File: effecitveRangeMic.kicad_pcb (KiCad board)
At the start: 2 copper layers, 24.4 x 18 mm, 25 parts, among them J1 MicHeader

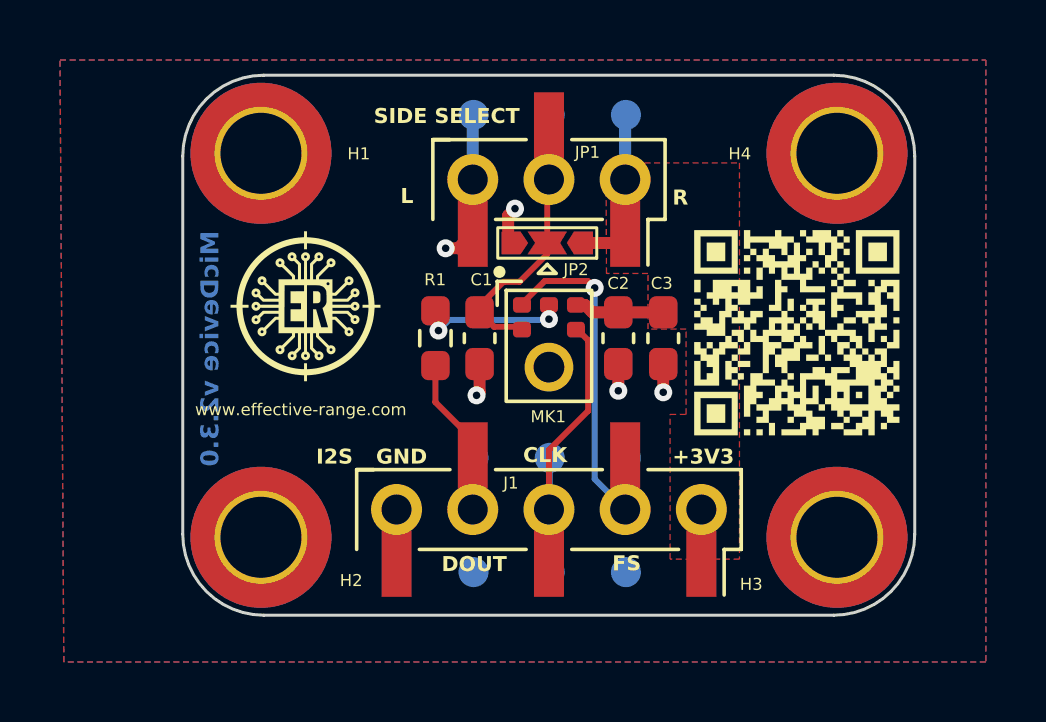
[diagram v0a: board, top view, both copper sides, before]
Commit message: Bumping release from 2.3.0 to 2.3.1
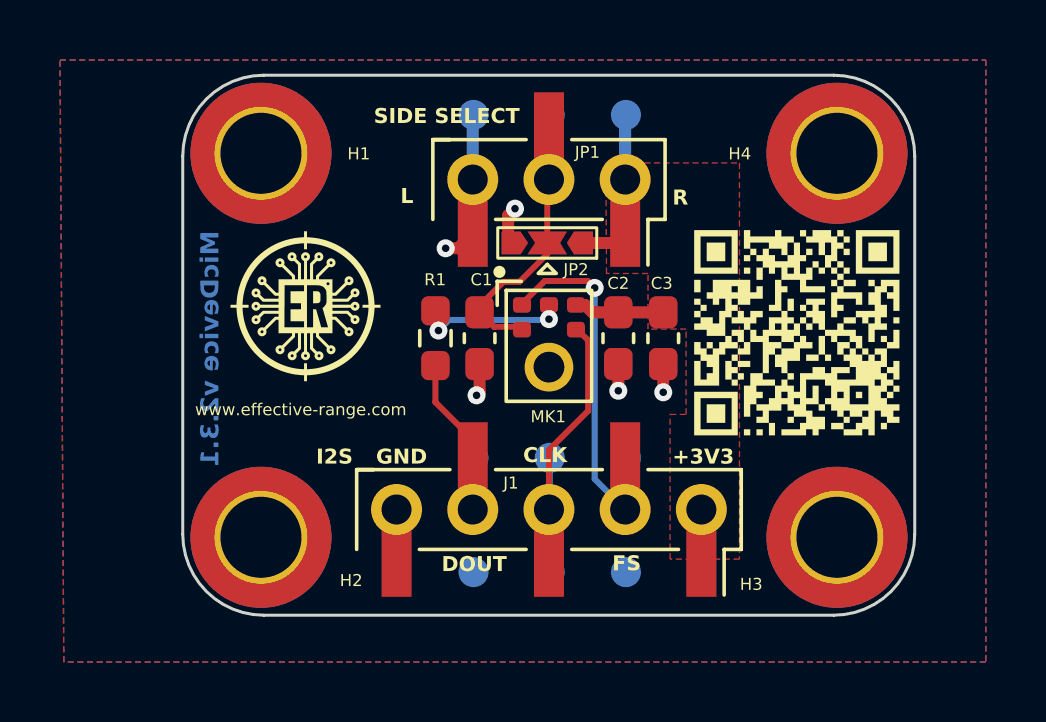
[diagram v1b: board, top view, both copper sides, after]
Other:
- board text added: "MicDevice v2.3.1"
- board text removed: "MicDevice v2.3.0"
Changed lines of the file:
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@@
 	(title_block
 		(title "Effective Range  Mic")
-		(date "2024-07-24")
-		(rev "2.3.0")
+		(date "2024-10-06")
+		(rev "2.3.1")
 		(company "Global Scope Ltd")
 		(comment 1 "Author: Ferenc Janky")
@@
 		(layer "Edge.Cuts")
 	)
-	(gr_text "MicDevice v2.3.0"
+	(gr_text "MicDevice v2.3.1"
 		(at 119.9896 60.9346 90)
 		(layer "B.Cu")
